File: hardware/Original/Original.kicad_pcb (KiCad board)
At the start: 2 copper layers, 102.1 x 16 mm, 59 parts, among them J2 Battery, J3 GPIO, J4 USB_B_Micro, J5 Power, J6 LEDs, J7 GPIO, Q1 BSS806N, Q2 BSS806N, Q3 BSS806N, Q4 BSS806N, SW1 Mode, SW2 Power, U1 STM32F411CE, U2 AP2210N-3.3TRG1, U3 MCP73830, U4 ESD7002WTT1G, U5 GD25Q16CEIGR, Y1 24Mhz

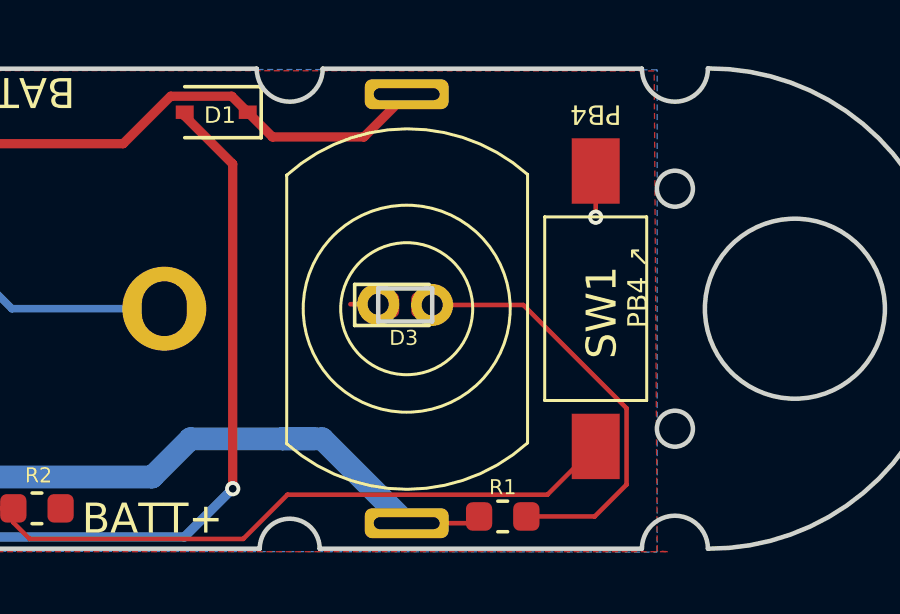
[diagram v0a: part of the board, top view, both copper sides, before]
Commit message: Update KAN15 LED placement.
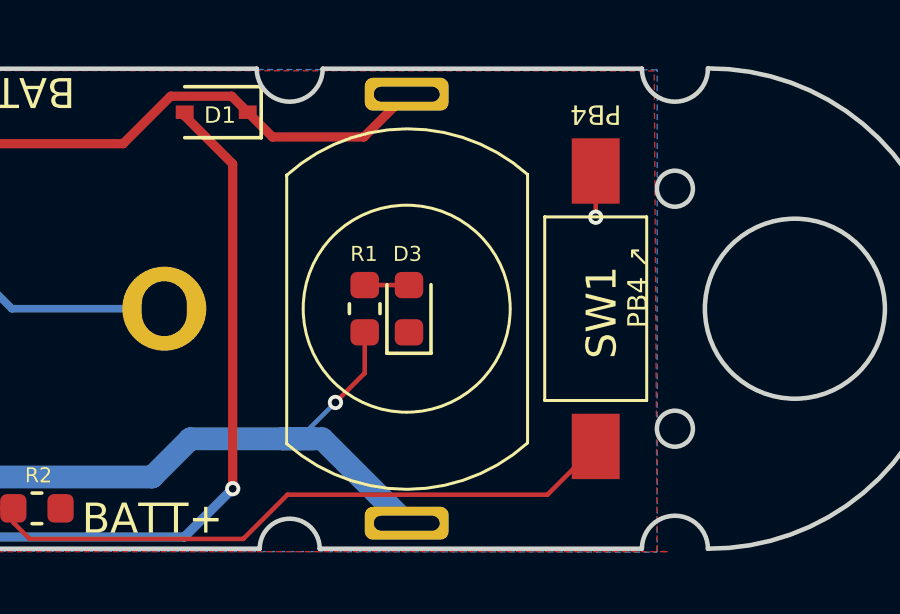
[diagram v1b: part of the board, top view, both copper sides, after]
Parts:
- removed REF** (x2): Pin_D0.7mm_L6.5mm_W1.8mm_FlatFork, Connector_Pin:Pin_D0.7mm_L6.5mm_W1.8mm_FlatFork
- D3: footprint LED_SMD:LED_0603_1608Metric_Castellated -> LED_SMD:LED_0603_1608Metric
- moved R1 8.31 mm to (140.7, 100.0), turned to 270 degrees
- moved D3 0.18 mm to (142.2, 100.0), turned to 90 degrees
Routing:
- net Net-(D3-Pad2): track 13.9 -> 1.48 mm
- net /VIN: track 54.5 -> 56.4 mm, vias 1 -> 2
- net GND: track 59.3 -> 58.7 mm
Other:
- outline, holes or cut-outs redrawn

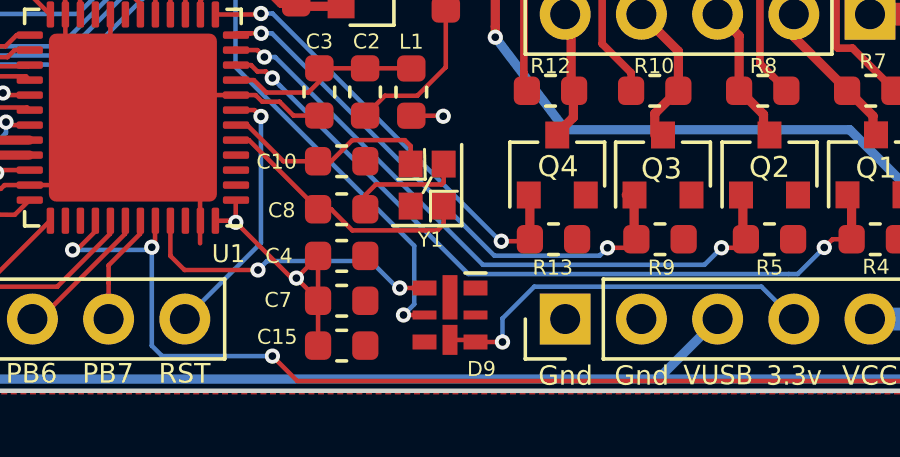
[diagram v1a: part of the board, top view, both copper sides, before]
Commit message: Fix kicad references.
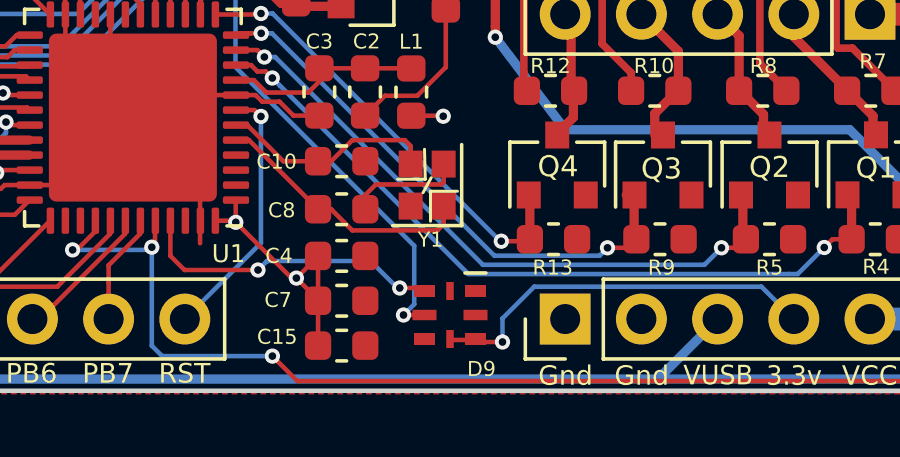
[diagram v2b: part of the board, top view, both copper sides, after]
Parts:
- D9: footprint LED_SMD:LED-APA102-2020 -> Jeremy LEDs:LED-APA102-2020

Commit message: v1.2
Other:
- board text added: "v1.2"
- board text removed: "v1.2a4"
